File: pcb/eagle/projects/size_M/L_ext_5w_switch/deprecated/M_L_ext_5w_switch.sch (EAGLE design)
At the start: 4 parts

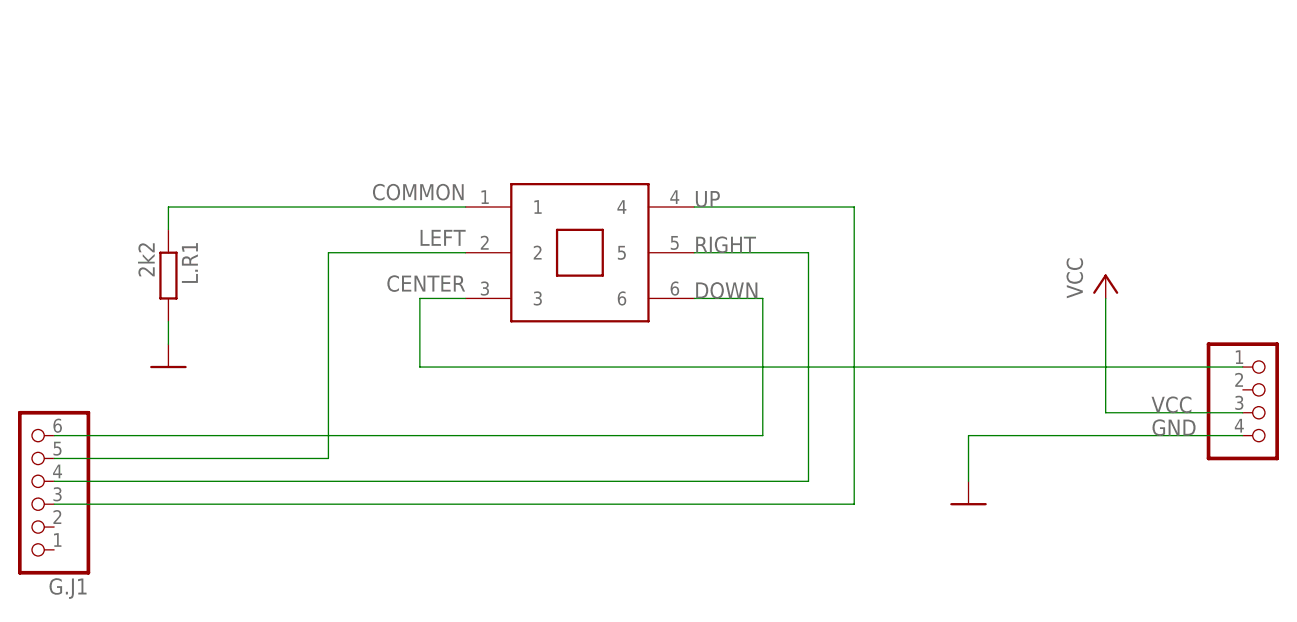
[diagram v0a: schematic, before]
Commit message: 5way switch - used 5 inputs
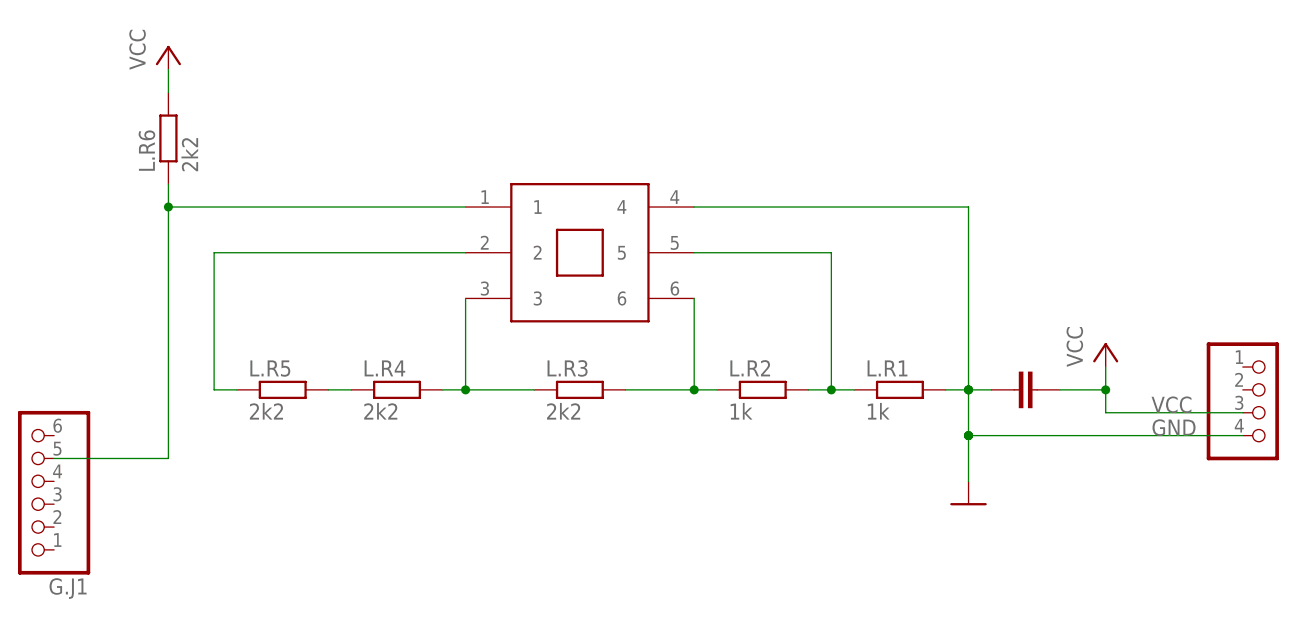
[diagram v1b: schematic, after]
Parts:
- added L.C1: 100n, rcl:C-EUC0603
- added L.R2: 1k, rcl:R-EU_R0603
- added L.R3, L.R4, L.R5, L.R6: 2k2, rcl:R-EU_R0603
- L.R1: value 2k2 -> 1k
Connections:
- removed net CENTER: G.J2.1, L.SW1.3
- removed net COMMON: L.R1.1, L.SW1.1
- removed net DOWN: G.J1.6, L.SW1.6
- removed net LEFT: G.J1.5, L.SW1.2
- removed net RIGHT: G.J1.4, L.SW1.5
- removed net UP: G.J1.3, L.SW1.4
- new net N$1: L.R4.1, L.R5.1
- new net N$4: L.R1.1, L.R2.2, L.SW1.5
- new net N$5: L.R2.1, L.R3.2, L.SW1.6
- new net N$6: L.R3.1, L.R4.2, L.SW1.3
- new net N$7: G.J1.5, L.R6.1, L.SW1.1
- new net N$8: L.R5.2, L.SW1.2
- net GND: now also L.C1.1, L.SW1.4
- net VCC: now also L.C1.2, L.R6.2
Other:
- moved on the sheet: L.R1
